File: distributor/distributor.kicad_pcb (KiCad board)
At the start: 2 copper layers, 91.5 x 52 mm, 38 parts, among them J1 Cerebellum, J10 CAN FD, J11 CAN FD, J12 CAN FD, J13 CAN FD, J14 ArmR, J15 CAN FD, J16 ArmL, J2 Cerebrum, J3 PowerIO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

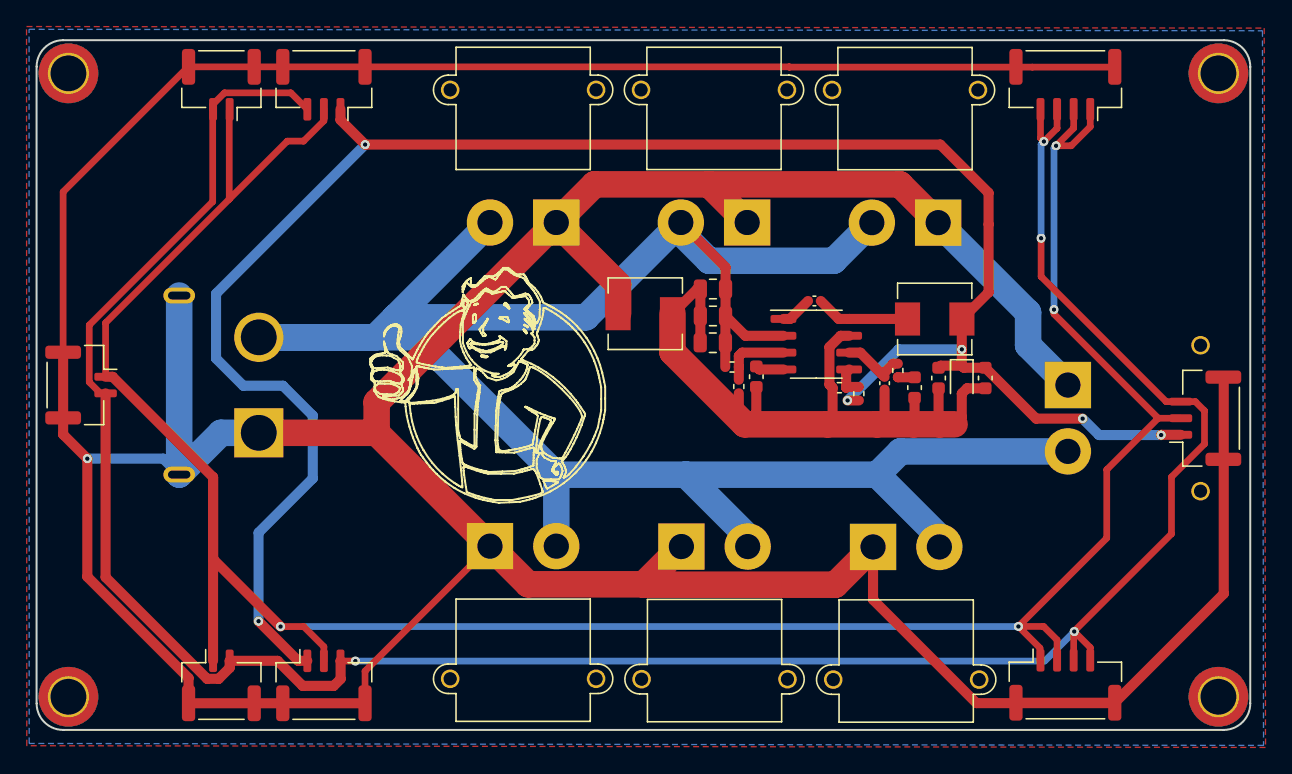
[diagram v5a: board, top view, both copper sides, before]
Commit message: [Fix] Correct distributor layout
Signed-off-by: Homalozoa <nx.tardis@gmail.com>
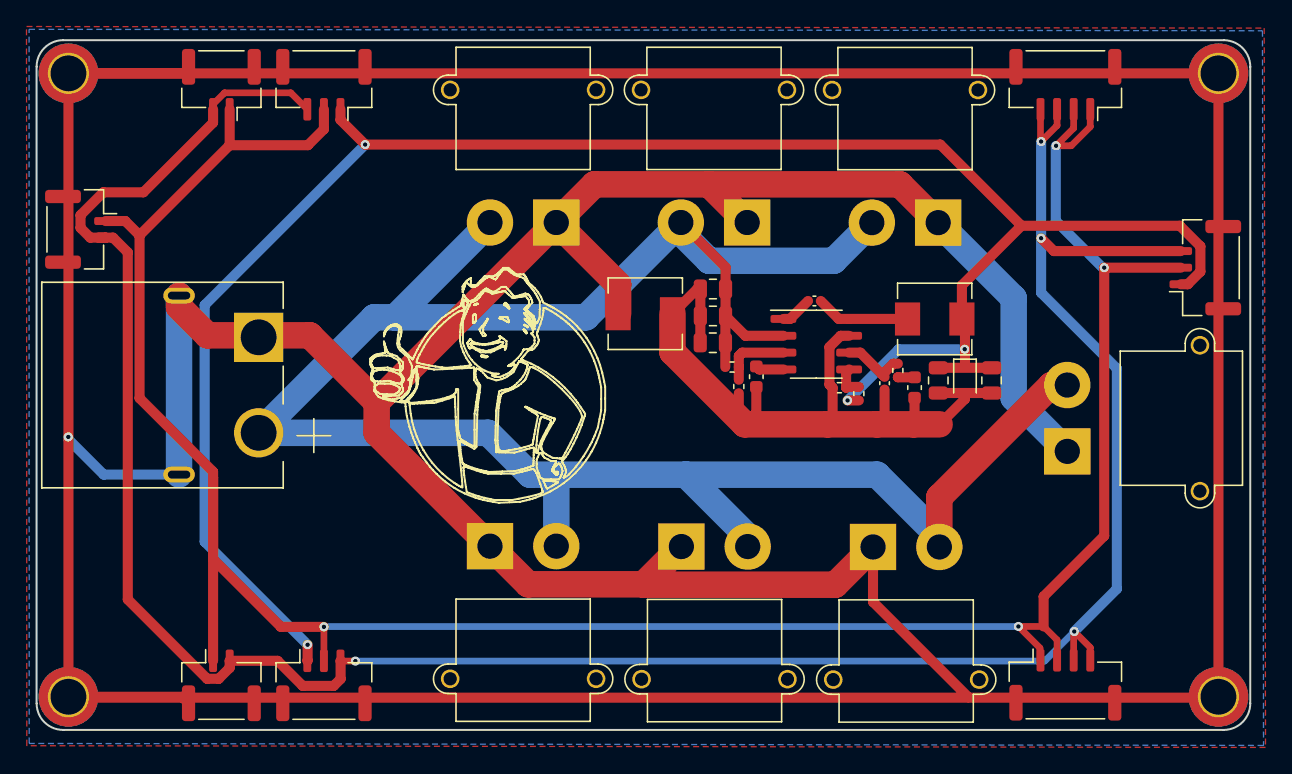
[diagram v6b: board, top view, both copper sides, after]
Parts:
- C8, C9: value 47uf/50V/0603 -> 47uf/6.3V/0805; footprint Capacitor_SMD:C_0603_1608Metric -> Capacitor_SMD:C_0805_2012Metric
- J3, J9: moved to F.Cu
- moved J10 11.7 mm to (107.6, 88.3)
- moved J4 11.4 mm to (192.4, 91.2)
- moved J3 5.00 mm to (182.0, 105.0), turned to -90 degrees
- moved C9 0.51 mm to (176.2, 99.7)
- moved D1 0.24 mm to (174.2, 99.5)
- moved C8 0.18 mm to (172.2, 99.7)
- turned J9 to 90 degrees
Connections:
- Mount2 pad 1: (no net) -> GNDA
- Mount3 pad 1: (no net) -> GNDA
- Mount4 pad 1: (no net) -> GNDA (x2)
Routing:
- net GNDA: track 381.9 -> 475.6 mm
- net CANFD_L: track 186.3 -> 194.1 mm
- net CANFD_H: track 195.1 -> 191.8 mm
- net +24V: track 166.2 -> 168.0 mm
- net +5V: track 149.3 -> 148.0 mm, vias 6 -> 4
- net GND: track 59.1 -> 57.9 mm

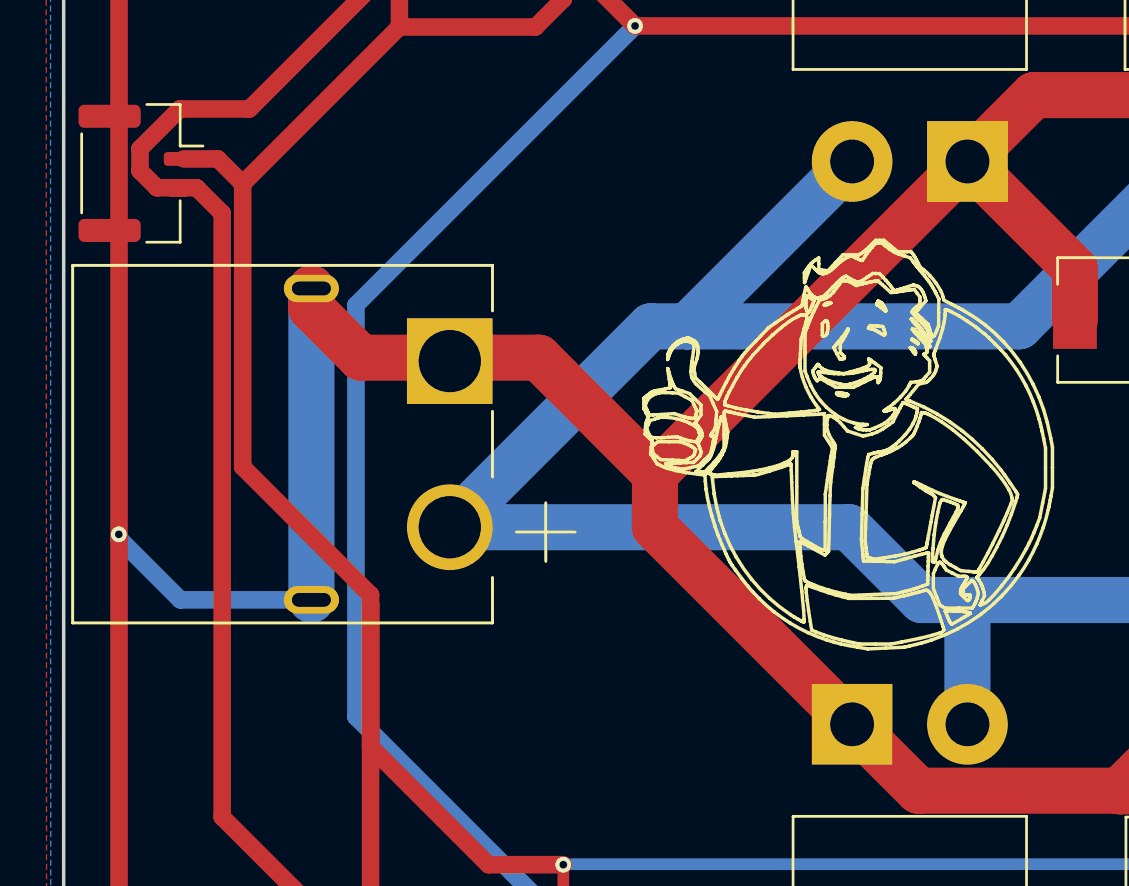
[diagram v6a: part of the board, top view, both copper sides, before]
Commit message: [Fix] Connect mounting hole to GNDA
Signed-off-by: Homalozoa <nx.tardis@gmail.com>
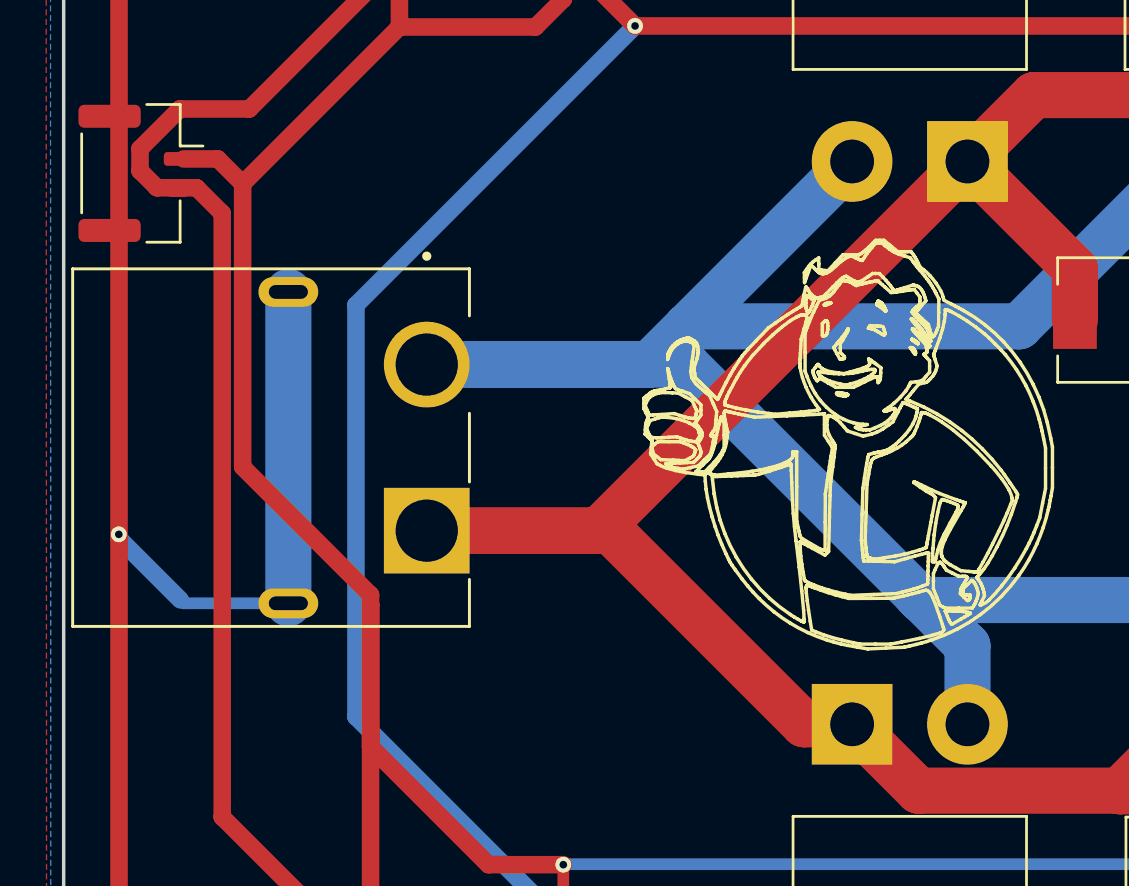
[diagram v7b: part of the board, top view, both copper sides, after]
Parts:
- J3: value PowerIO -> PowerBack
- J9: footprint Rolling_Custom:AMASS_XT60PW-M -> Rolling_Custom:AMASS_XT60PW-F
- moved J9 1.16 mm to (113.8, 100.0)
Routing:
- net +24V: track 168.0 -> 171.2 mm
- net GNDA: track 475.6 -> 474.4 mm

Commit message: [Modify] Change CAN ports sequence
2pin: 1-CAN_L, 2-CAN_H
3pin: 1-5V, 2-CAN_L, 3-CAN_H
4pin: 1,2-CAN_L, 3,4-CAN_H

Signed-off-by: Homalozoa <nx.tardis@gmail.com>
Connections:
- J10 pad 1: CANFD_H -> CANFD_L
- J10 pad 2: CANFD_L -> CANFD_H
- J11 pad 1: CANFD_H -> CANFD_L
- J11 pad 2: CANFD_L -> CANFD_H
- J12 pad 1: CANFD_H -> CANFD_L
- J12 pad 2: CANFD_L -> CANFD_H
- J13 pad 1: CANFD_H -> CANFD_L
- J13 pad 2: CANFD_H -> CANFD_L
- J13 pad 3: CANFD_L -> CANFD_H
- J13 pad 4: CANFD_L -> CANFD_H
- J14 pad 2: CANFD_H -> CANFD_L
- J14 pad 3: CANFD_L -> CANFD_H
- J15 pad 1: CANFD_H -> CANFD_L
- J15 pad 2: CANFD_H -> CANFD_L
- J15 pad 3: CANFD_L -> CANFD_H
- J15 pad 4: CANFD_L -> CANFD_H
- J16 pad 2: CANFD_H -> CANFD_L
- J16 pad 3: CANFD_L -> CANFD_H
- J4 pad 2: CANFD_H -> CANFD_L
- J4 pad 3: CANFD_L -> CANFD_H
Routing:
- net CANFD_L: track 194.1 -> 191.8 mm
- net CANFD_H: track 191.8 -> 194.1 mm
